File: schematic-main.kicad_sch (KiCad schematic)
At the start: 10 parts, among them J1 Fell_Cell_Conn_01x02_Pin, J2 Conn_01x02, J3 Conn_01x02, J4 Conn_01x03, J6 Conn_01x03, P1 USB_C_Plug_USB2.0

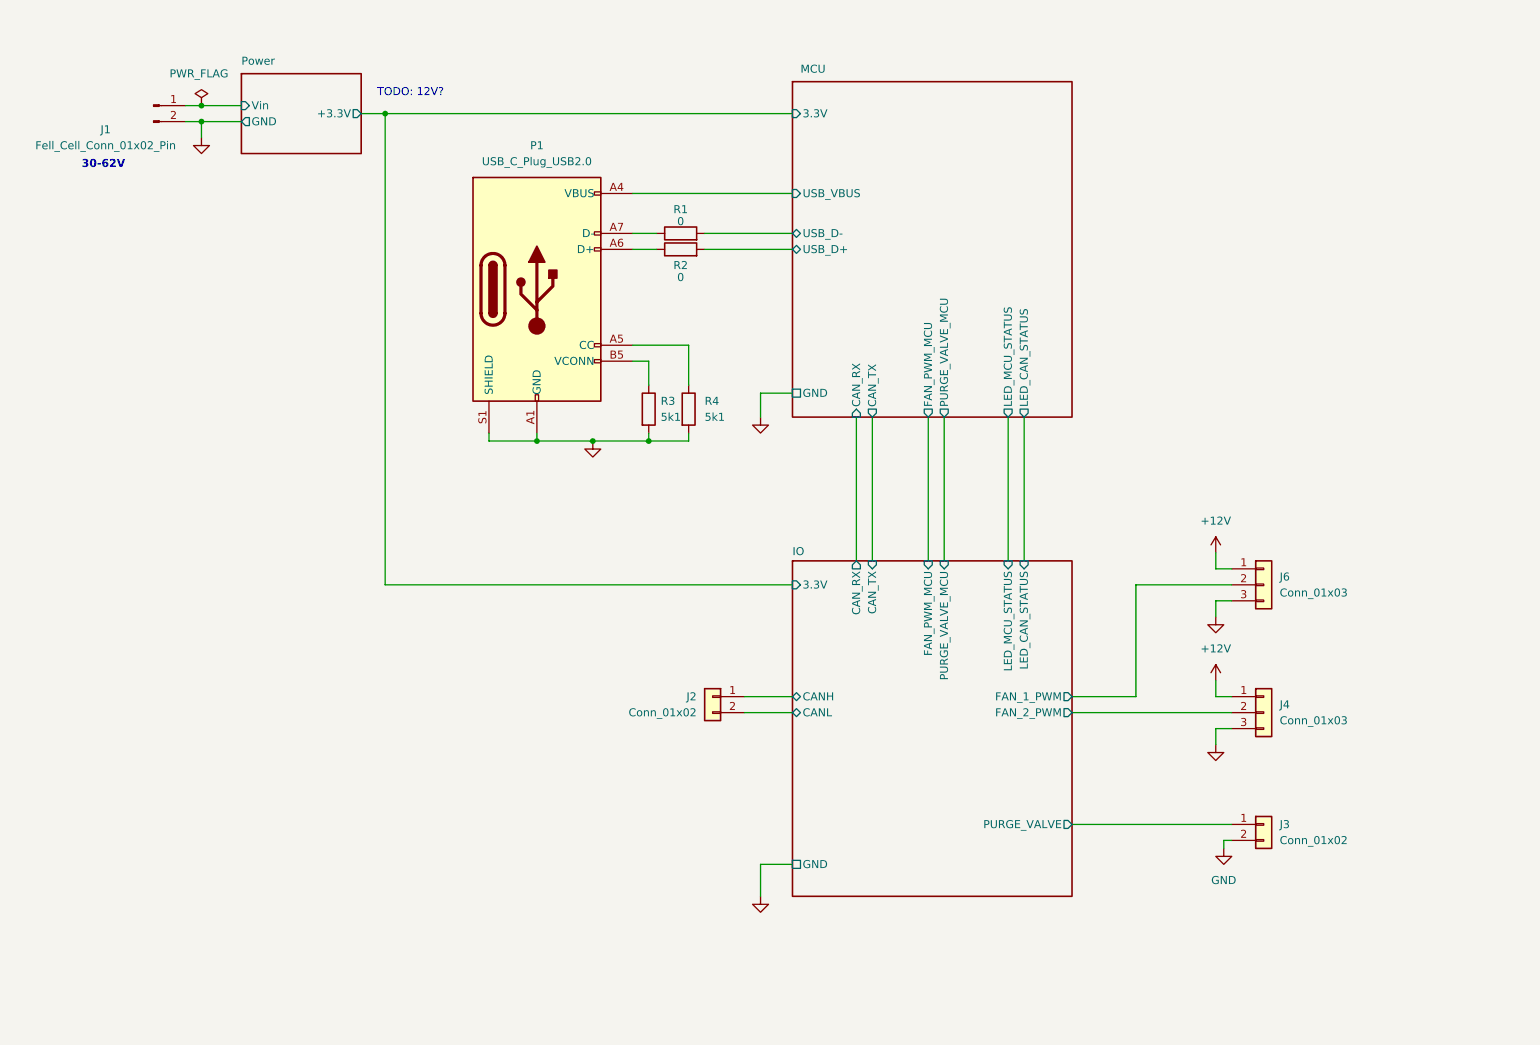
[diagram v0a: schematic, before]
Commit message: Add power stages
Valve, power supplay, fan
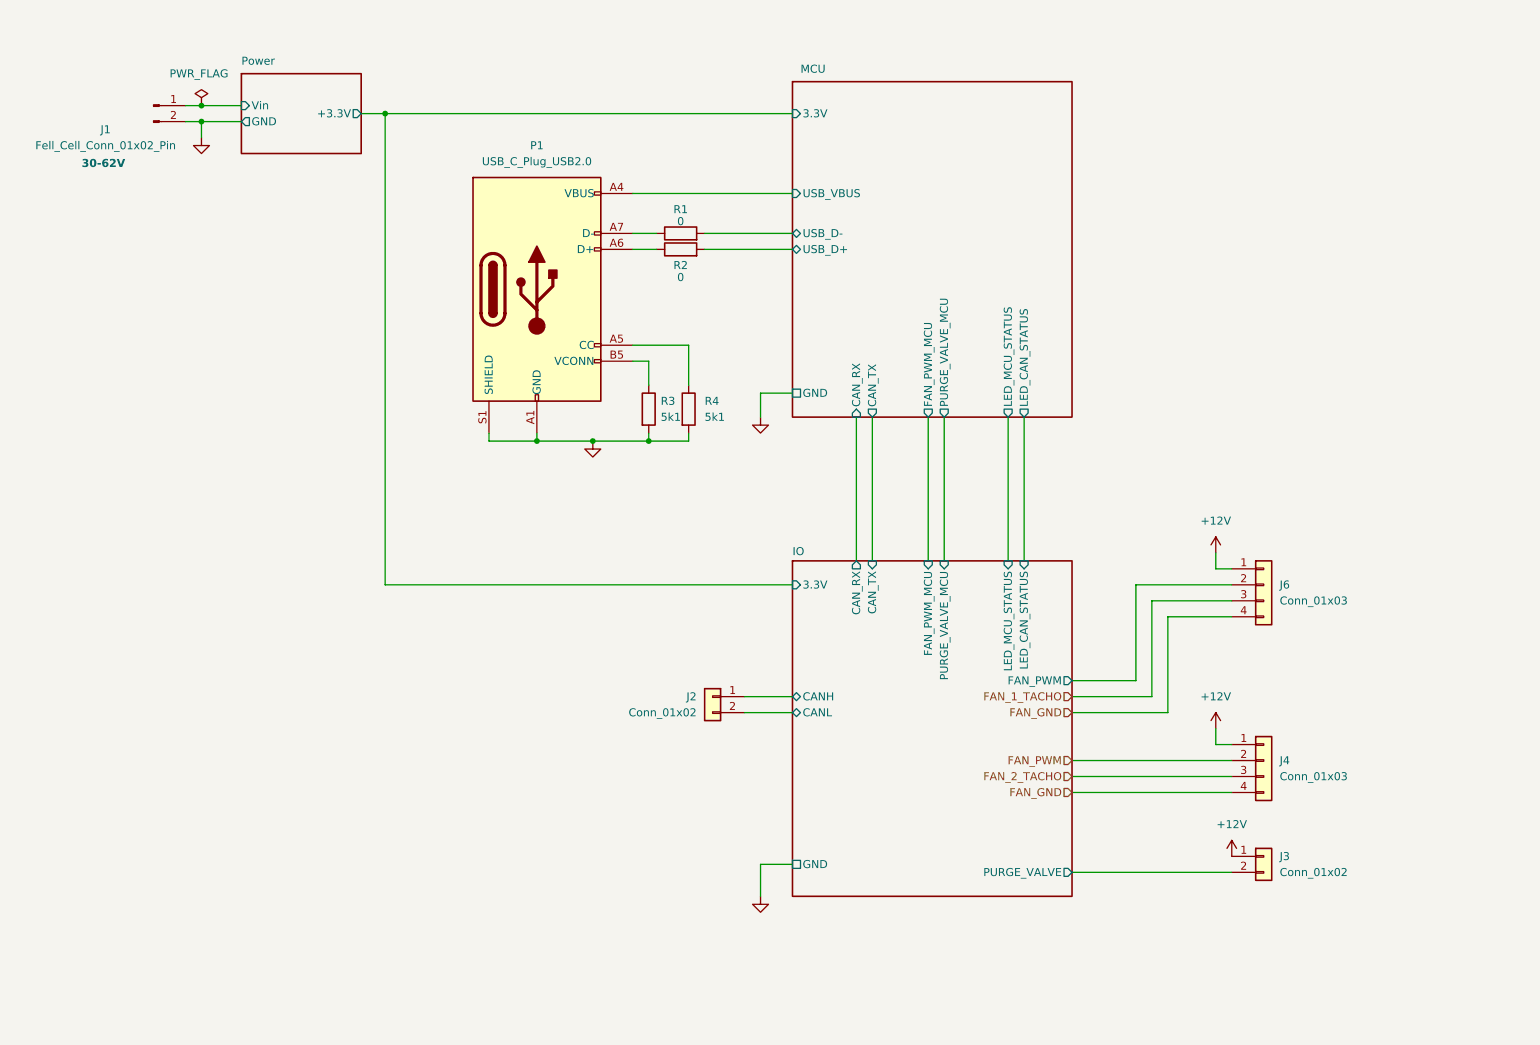
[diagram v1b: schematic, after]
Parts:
- J4, J6: symbol Connector_Generic:Conn_01x03 -> Connector_Generic:Conn_01x04
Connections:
- net +12V: now also J3.1 (Pin_1)
- net GND: no longer J3.2 (Pin_2), J4.3 (Pin_3), J6.3 (Pin_3)
- net IO/PURGE_VALVE: now also J3.2 (Pin_2); no longer J3.1 (Pin_1)
- net IO/FAN_1_PWM renamed IO/FAN_PWM
- net IO/FAN_2_PWM renamed FAN_PWM
- new net FAN_1_TACHO: J6.3 (Pin_3)
- new net FAN_2_TACHO: J4.3 (Pin_3)
- new net FAN_GND: J4.4 (Pin_4), J6.4 (Pin_4)
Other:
- sheet IO ports: added FAN_PWM; removed FAN_1_PWM, FAN_2_PWM
- note removed: "TODO: 12V?"
- moved on the sheet: J3

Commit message: Add tags
Edit main schema and sockets
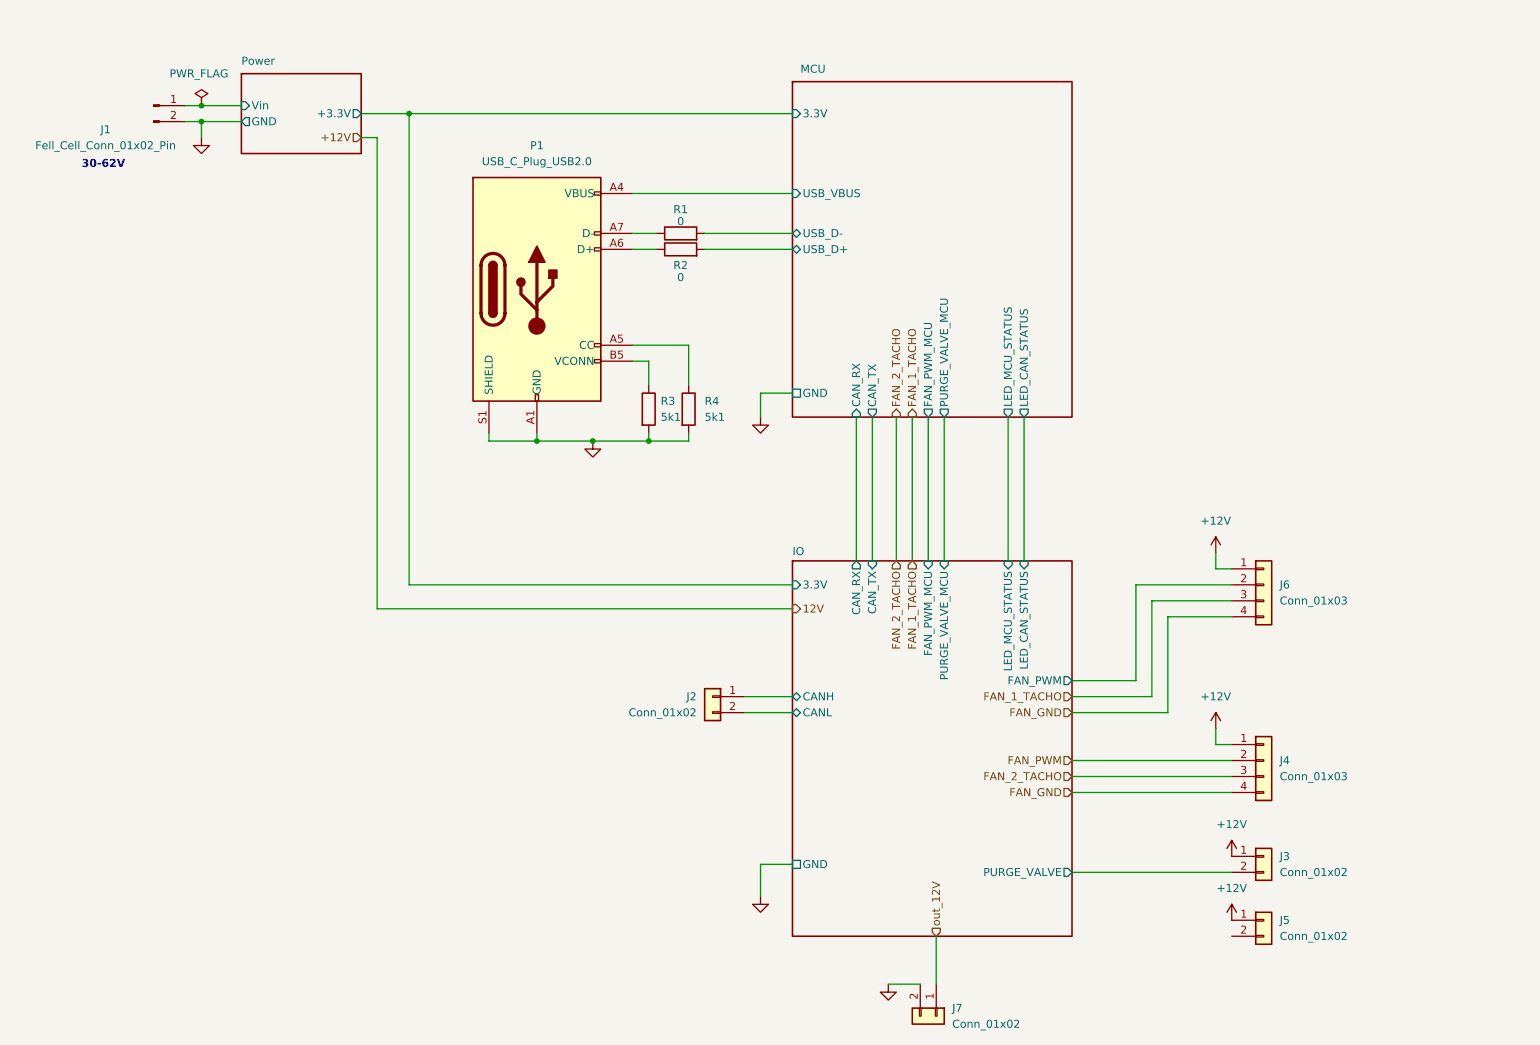
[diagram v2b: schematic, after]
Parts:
- added J5, J7: Conn_01x02, symbol Connector_Generic:Conn_01x02
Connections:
- net +12V: now also J5.1 (Pin_1)
- net GND: now also J7.2 (Pin_2)
- new net out_12V: J7.1 (Pin_1)
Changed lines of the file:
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@@
   (junction (at 102.87 85.09) (diameter 0) (color 0 0 0 0)
   )
-  (junction (at 69.85 33.02) (diameter 0) (color 0 0 0 0)
-  )
   (junction (at 93.98 85.09) (diameter 0) (color 0 0 0 0)
   )
   (junction (at 40.64 31.75) (diameter 0) (color 0 0 0 0)
   )
+  (junction (at 73.66 33.02) (diameter 0) (color 0 0 0 0)
+  )
   (junction (at 111.76 85.09) (diameter 0) (color 0 0 0 0)
   )
@@
     (stroke (width 0) (type default))
   )
+  (wire (pts (xy 153.67 81.28) (xy 153.67 104.14))
+    (stroke (width 0) (type default))
+  )
+  (wire (pts (xy 157.48 163.83) (xy 157.48 171.45))
+    (stroke (width 0) (type default))
+  )
   (wire (pts (xy 102.87 85.09) (xy 93.98 85.09))
     (stroke (width 0) (type default))
   )
+  (wire (pts (xy 68.58 36.83) (xy 68.58 111.76))
+    (stroke (width 0) (type default))
+  )
   (wire (pts (xy 156.21 81.28) (xy 156.21 104.14))
     (stroke (width 0) (type default))
@@
     (stroke (width 0) (type default))
   )
-  (wire (pts (xy 69.85 33.02) (xy 134.62 33.02))
-    (stroke (width 0) (type default))
-  )
   (wire (pts (xy 204.47 133.35) (xy 201.93 133.35))
     (stroke (width 0) (type default))
@@
     (stroke (width 0) (type default))
   )
-  (wire (pts (xy 69.85 107.95) (xy 134.62 107.95))
+  (wire (pts (xy 73.66 107.95) (xy 134.62 107.95))
     (stroke (width 0) (type default))
   )
@@
     (stroke (width 0) (type default))
   )
-  (wire (pts (xy 66.04 33.02) (xy 69.85 33.02))
+  (wire (pts (xy 151.13 81.28) (xy 151.13 104.14))
+    (stroke (width 0) (type default))
+  )
+  (wire (pts (xy 68.58 111.76) (xy 134.62 111.76))
     (stroke (width 0) (type default))
   )
@@
     (stroke (width 0) (type default))
   )
+  (wire (pts (xy 73.66 33.02) (xy 134.62 33.02))
+    (stroke (width 0) (type default))
+  )
   (wire (pts (xy 109.22 69.85) (xy 118.11 69.85))
     (stroke (width 0) (type default))
@@
     (stroke (width 0) (type default))
   )
+  (wire (pts (xy 149.86 171.45) (xy 154.94 171.45))
+    (stroke (width 0) (type default))
+  )
   (wire (pts (xy 127 128.27) (xy 134.62 128.27))
     (stroke (width 0) (type default))
   )
+  (wire (pts (xy 66.04 33.02) (xy 73.66 33.02))
+    (stroke (width 0) (type default))
+  )
   (wire (pts (xy 179.07 140.97) (xy 204.47 140.97))
     (stroke (width 0) (type default))
@@
     (stroke (width 0) (type default))
   )
-  (wire (pts (xy 69.85 33.02) (xy 69.85 107.95))
+  (wire (pts (xy 73.66 33.02) (xy 73.66 107.95))
     (stroke (width 0) (type default))
   )
   (wire (pts (xy 40.64 34.29) (xy 40.64 36.83))
+    (stroke (width 0) (type default))
+  )
+  (wire (pts (xy 66.04 36.83) (xy 68.58 36.83))
     (stroke (width 0) (type default))
   )
@@
     (effects (font (size 1.27 1.27) (thickness 0.254) bold) (justify left bottom))
   )
+  (hierarchical_label "out_12V" (shape input) (at 157.48 163.83 90) (fields_autoplaced)
+    (effects (font (size 1.27 1.27)) (justify left))
+  )
+  (hierarchical_label "FAN_2_TACHO" (shape input) (at 151.13 104.14 270) (fields_autoplaced)
+    (effects (font (size 1.27 1.27)) (justify right))
+  )
   (hierarchical_label "FAN_GND" (shape input) (at 179.07 128.27 180) (fields_autoplaced)
     (effects (font (size 1.27 1.27)) (justify right))
@@
     (effects (font (size 1.27 1.27)) (justify right))
   )
+  (hierarchical_label "FAN_1_TACHO" (shape output) (at 153.67 81.28 90) (fields_autoplaced)
+    (effects (font (size 1.27 1.27)) (justify left))
+  )
+  (hierarchical_label "12V" (shape output) (at 134.62 111.76 0) (fields_autoplaced)
+    (effects (font (size 1.27 1.27)) (justify left))
+  )
+  (hierarchical_label "FAN_1_TACHO" (shape input) (at 153.67 104.14 270) (fields_autoplaced)
+    (effects (font (size 1.27 1.27)) (justify right))
+  )
+  (hierarchical_label "+12V" (shape input) (at 66.04 36.83 180) (fields_autoplaced)
+    (effects (font (size 1.27 1.27)) (justify right))
+  )
   (hierarchical_label "FAN_PWM" (shape input) (at 179.07 135.89 180) (fields_autoplaced)
     (effects (font (size 1.27 1.27)) (justify right))
@@
   (hierarchical_label "FAN_2_TACHO" (shape input) (at 179.07 138.43 180) (fields_autoplaced)
     (effects (font (size 1.27 1.27)) (justify right))
+  )
+  (hierarchical_label "FAN_2_TACHO" (shape output) (at 151.13 81.28 90) (fields_autoplaced)
+    (effects (font (size 1.27 1.27)) (justify left))
   )
   (symbol (lib_id "power:GND") (at 129.54 157.48 0) (unit 1)
@@
     )
   )
+  (symbol (lib_id "power:GND") (at 149.86 171.45 0) (unit 1)
+    (in_bom yes) (on_board yes) (dnp no) (fields_autoplaced)
+    (property "Reference" "#PWR067" (at 149.86 177.8 0)
+      (effects (font (size 1.27 1.27)) hide)
+    )
+    (property "Value" "GND" (at 149.86 176.53 0)
+      (effects (font (size 1.27 1.27)) hide)
+    )
+    (property "Footprint" "" (at 149.86 171.45 0)
+      (effects (font (size 1.27 1.27)) hide)
+    )
+    (property "Datasheet" "" (at 149.86 171.45 0)
+      (effects (font (size 1.27 1.27)) hide)
+    )
+    (pin "1")
+    (instances
+      (project "schematic-main"
+        (path "/c9ad7189-d3b2-414a-9743-efd8e57cd755"
+          (reference "#PWR067") (unit 1)
+        )
+      )
+    )
+  )
   (symbol (lib_id "Connector_Generic:Conn_01x04") (at 209.55 107.95 0) (unit 1)
     (in_bom yes) (on_board yes) (dnp no) (fields_autoplaced)
@@
     )
   )
+  (symbol (lib_id "power:+12V") (at 204.47 161.29 0) (unit 1)
+    (in_bom yes) (on_board yes) (dnp no)
+    (property "Reference" "#PWR065" (at 204.47 165.1 0)
+      (effects (font (size 1.27 1.27)) hide)
+    )
+    (property "Value" "+12V" (at 204.47 156.21 0)
+      (effects (font (size 1.27 1.27)))
+    )
+    (property "Footprint" "" (at 204.47 161.29 0)
+      (effects (font (size 1.27 1.27)) hide)
+    )
+    (property "Datasheet" "" (at 204.47 161.29 0)
+      (effects (font (size 1.27 1.27)) hide)
+    )
+    (pin "1")
+    (instances
+      (project "schematic-main"
+        (path "/c9ad7189-d3b2-414a-9743-efd8e57cd755"
+          (reference "#PWR065") (unit 1)
+        )
+      )
+    )
+  )
   (symbol (lib_id "Connector_Generic:Conn_01x02") (at 121.92 125.73 0) (mirror y) (unit 1)
     (in_bom yes) (on_board yes) (dnp no)
@@
     )
   )
+  (symbol (lib_id "Connector_Generic:Conn_01x02") (at 157.48 176.53 270) (unit 1)
+    (in_bom yes) (on_board yes) (dnp no) (fields_autoplaced)
+    (property "Reference" "J7" (at 160.02 175.26 90)
+      (effects (font (size 1.27 1.27)) (justify left))
+    )
+    (property "Value" "Conn_01x02" (at 160.02 177.8 90)
+      (effects (font (size 1.27 1.27)) (justify left))
+    )
+    (property "Footprint" "" (at 157.48 176.53 0)
+      (effects (font (size 1.27 1.27)) hide)
+    )
+    (property "Datasheet" "~" (at 157.48 176.53 0)
+      (effects (font (size 1.27 1.27)) hide)
+    )
+    (pin "1")
+    (pin "2")
+    (instances
+      (project "schematic-main"
+        (path "/c9ad7189-d3b2-414a-9743-efd8e57cd755"
+          (reference "J7") (unit 1)
+        )
+      )
+    )
+  )
   (symbol (lib_id "Connector:Conn_01x02_Pin") (at 33.02 31.75 0) (unit 1)
     (in_bom yes) (on_board yes) (dnp no)
@@
     )
   )
-  (sheet (at 134.62 104.14) (size 44.45 53.34) (fields_autoplaced)
+  (symbol (lib_id "Connector_Generic:Conn_01x02") (at 209.55 161.29 0) (unit 1)
+    (in_bom yes) (on_board yes) (dnp no) (fields_autoplaced)
+    (property "Reference" "J5" (at 212.09 161.29 0)
+      (effects (font (size 1.27 1.27)) (justify left))
+    )
+    (property "Value" "Conn_01x02" (at 212.09 163.83 0)
+      (effects (font (size 1.27 1.27)) (justify left))
+    )
+    (property "Footprint" "" (at 209.55 161.29 0)
+      (effects (font (size 1.27 1.27)) hide)
+    )
+    (property "Datasheet" "~" (at 209.55 161.29 0)
+      (effects (font (size 1.27 1.27)) hide)
+    )
+    (pin "1")
+    (pin "2")
+    (instances
+      (project "schematic-main"
+        (path "/c9ad7189-d3b2-414a-9743-efd8e57cd755"
+          (reference "J5") (unit 1)
+        )
+      )
+    )
+  )
+  (sheet (at 134.62 104.14) (size 44.45 59.69) (fields_autoplaced)
     (stroke (width 0.254) (type solid))
     (fill (color 255 255 154 1.0000))
@@
       (effects (font (size 1.27 1.27)) (justify left bottom))
     )
-    (property "Sheetfile" "schematc-io.kicad_sch" (at 134.62 158.1154 0)
+    (property "Sheetfile" "schematc-io.kicad_sch" (at 134.62 164.4654 0)
       (effects (font (size 1.27 1.27)) (justify left top) hide)
     )
